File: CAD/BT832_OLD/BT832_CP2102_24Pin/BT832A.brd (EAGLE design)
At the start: 24.9 x 49.9 mm, 44 parts, among them IC1 CP2102, U1 MCP73831T-3ACI/OT, U2 BT832, U3 LP5907MFX-3.3/NOPB, U4 LP5907MFX-3.3/NOPB, U5 ADS131M08IPBS, U6 BCM857BS, X1 ABM3B-8.000MHZ-B2-T, X2 FC-12M

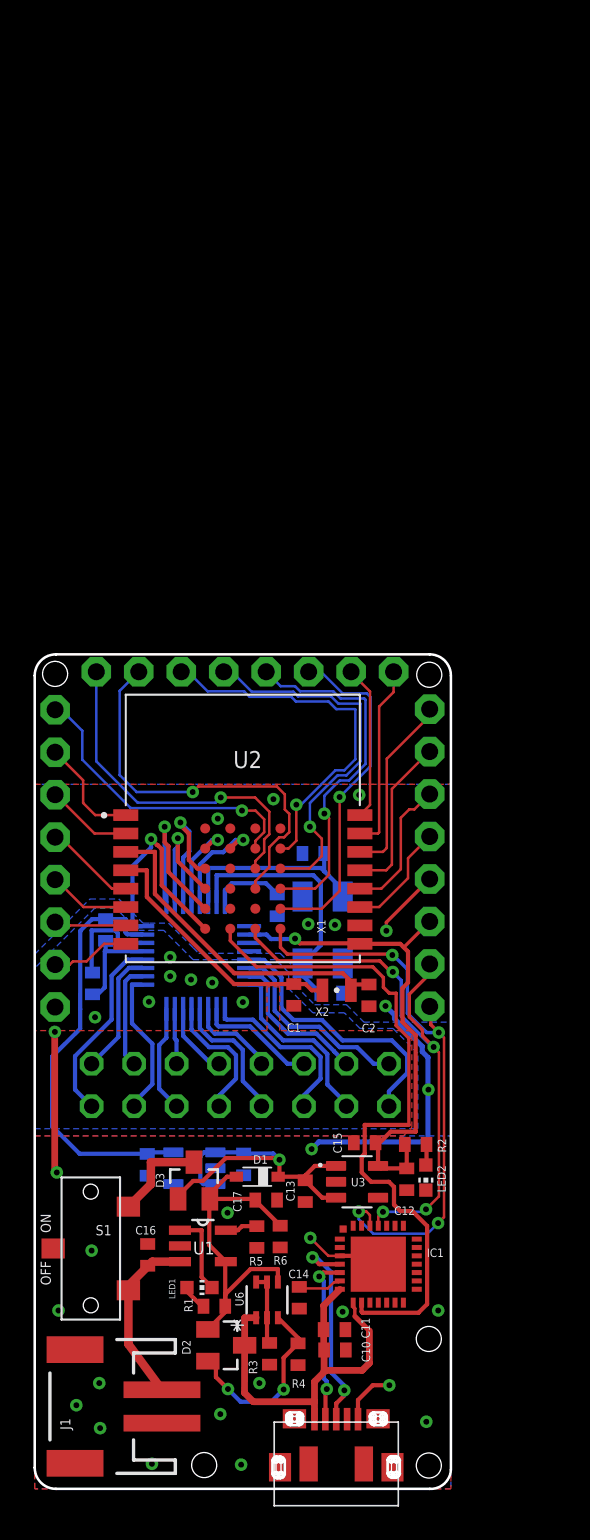
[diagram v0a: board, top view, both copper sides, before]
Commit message: added missing voltage divider (doesn't fix the battery charger circuit)
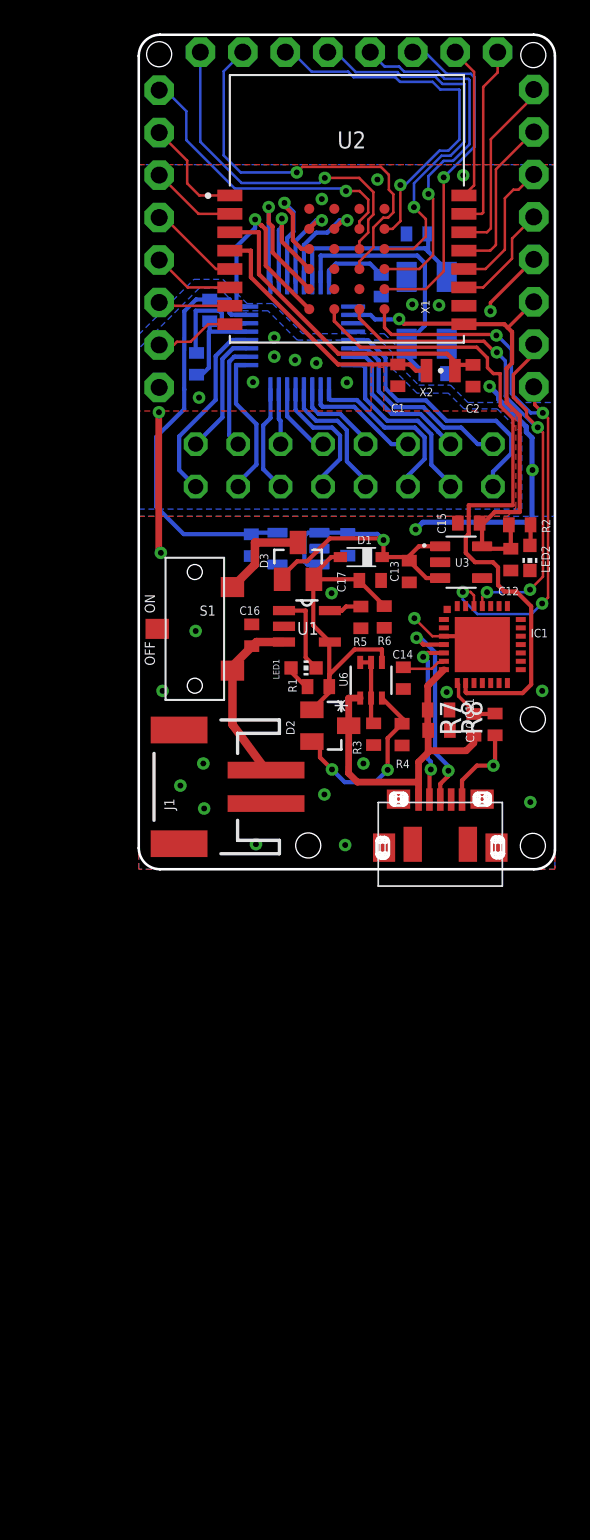
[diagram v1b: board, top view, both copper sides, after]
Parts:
- added R7: 24kΩ, adafruit:R0402
- added R8: 47kΩ, adafruit:R0402
- moved C3 37.6 mm to (30.6, 37.6)
- moved C1 37.6 mm to (28.3, 37.5)
- moved C10 37.6 mm to (30.8, 16.3)
- moved C11 37.6 mm to (30.8, 17.5)
- moved C12 37.6 mm to (35.1, 26.5)
- moved C13 37.6 mm to (29.0, 25.8)
- moved C14 37.6 mm to (28.7, 19.4)
- moved C15 37.6 mm to (32.6, 28.7)
- moved C16 37.6 mm to (19.6, 22.0)
- moved C17 37.6 mm to (26.7, 25.2)
- moved C2 37.6 mm to (32.8, 37.5)
- moved C4 37.6 mm to (29.5, 46.0)
- moved C5 37.6 mm to (17.1, 41.4)
- moved C6 37.6 mm to (27.3, 42.9)
- moved C7 37.6 mm to (25.3, 27.4)
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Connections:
- new net VBUS: IC1.8, R7.2, R8.2
- net +5V: now also R7.1; no longer IC1.8
- net GND: now also R8.1
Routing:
- net +5V: track 25.0 -> 21.4 mm
- net VBUS: track 0.00 -> 3.54 mm
- net GND: track 43.1 -> 44.9 mm
